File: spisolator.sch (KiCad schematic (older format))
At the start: 8 parts, among them P1 CONN_01X06, P2 CONN_02X04, U1 4066, U2 SPI_TGT

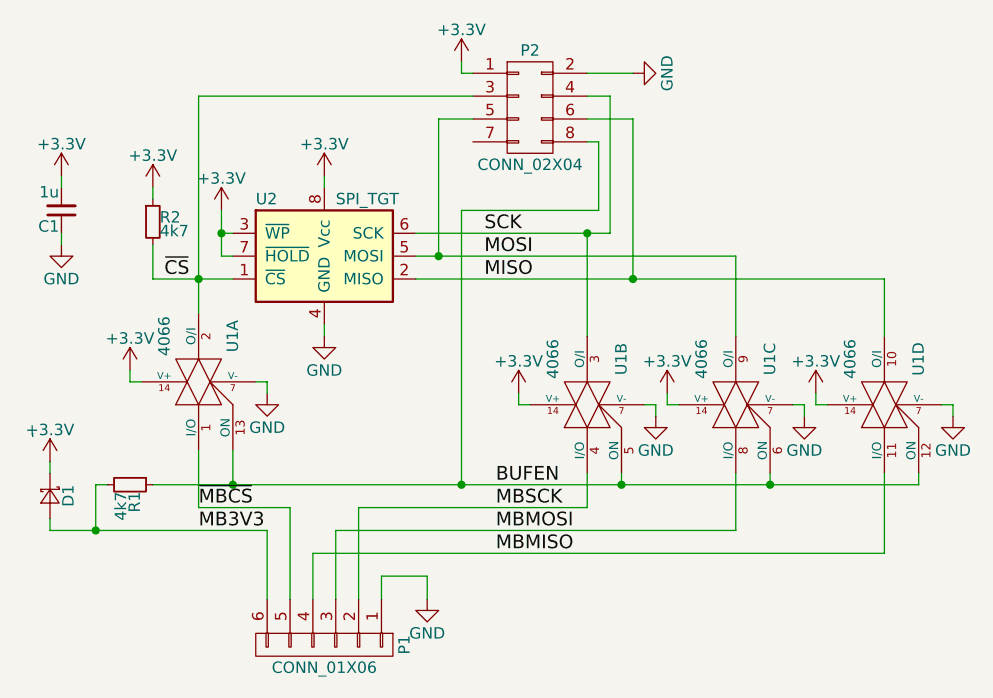
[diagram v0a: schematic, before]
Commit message: Fix swapped MISO/MOSI in the programming connector
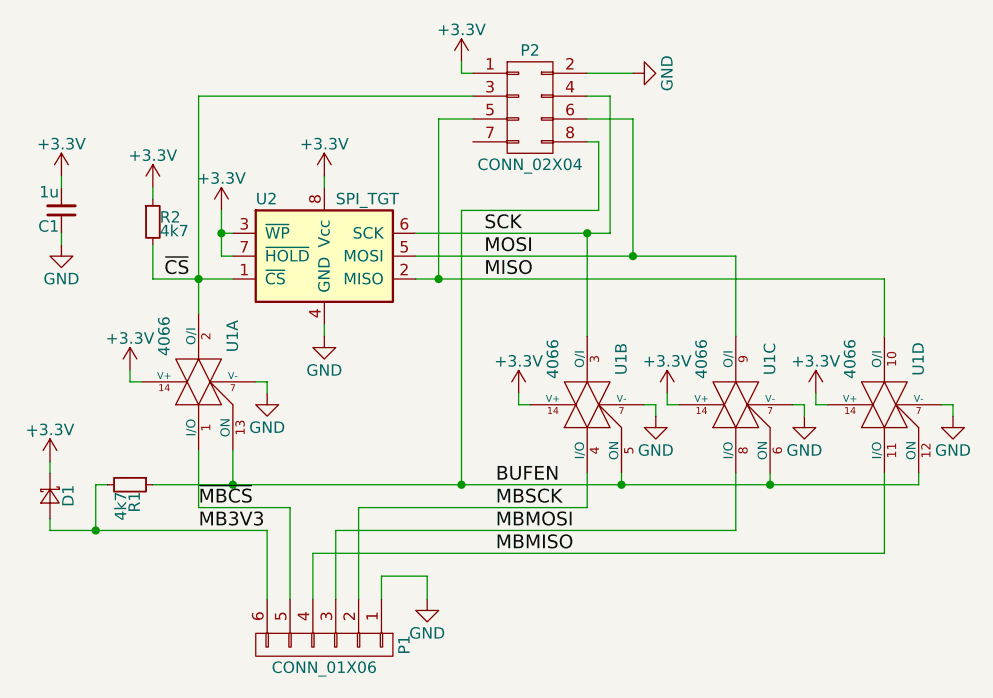
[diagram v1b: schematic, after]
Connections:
- net MISO: now also P2.5 (P5); no longer P2.6 (P6)
- net MOSI: now also P2.6 (P6); no longer P2.5 (P5)
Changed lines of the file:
@@
 LIBS:contrib
 LIBS:valves
+LIBS:spisolator-cache
 EELAYER 25 0
 EELAYER END
@@
 	6000 3000 4800 3000
 Wire Wire Line
-	6000 3100 5850 3100
-Wire Wire Line
-	5850 3100 5850 3700
-Connection ~ 5850 3700
-Wire Wire Line
 	6500 3000 6600 3000
 Wire Wire Line
 	6600 3000 6600 3600
 Connection ~ 6500 3600
-Wire Wire Line
-	6500 3100 6700 3100
-Wire Wire Line
-	6700 3100 6700 3800
-Connection ~ 6700 3800
 Connection ~ 5950 4700
 $Comp
@@
 	4900 3700 4950 3700
 Connection ~ 4900 3600
+Wire Wire Line
+	5850 3800 5850 3100
+Wire Wire Line
+	5850 3100 6000 3100
+Connection ~ 5850 3800
+Wire Wire Line
+	6700 3700 6700 3100
+Wire Wire Line
+	6700 3100 6500 3100
+Connection ~ 6700 3700
 $EndSCHEMATC
